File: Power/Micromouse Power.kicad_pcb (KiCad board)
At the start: 2 copper layers, 44.7 x 28.4 mm, 56 parts, among them J1 Battery, J2 Conn_02x08_Odd_Even, Q1 AO3401A, Q2 AO3401A, SW1 pwr, SW2 pwr, U1 AMS1117-3.3, U2 TP4056, U3 DRV8837, U4 DRV8837

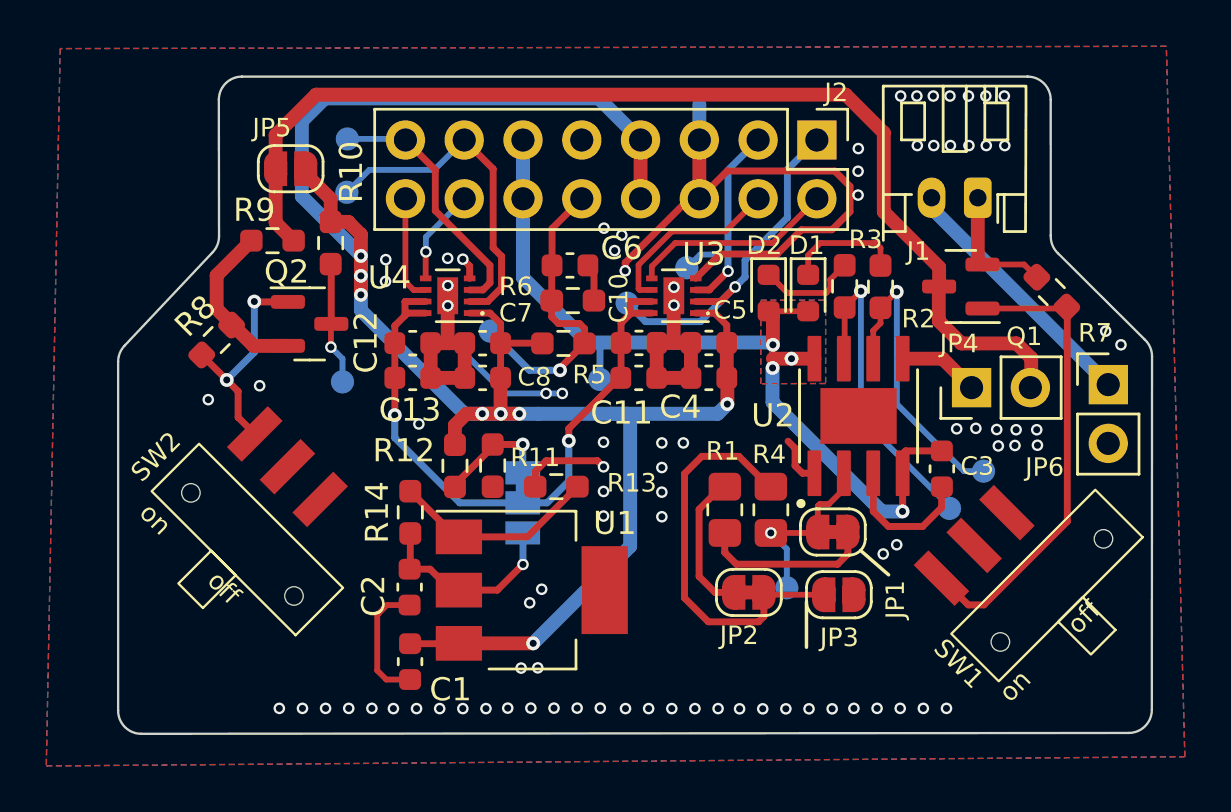
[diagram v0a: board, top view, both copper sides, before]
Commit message: Fixed tab width
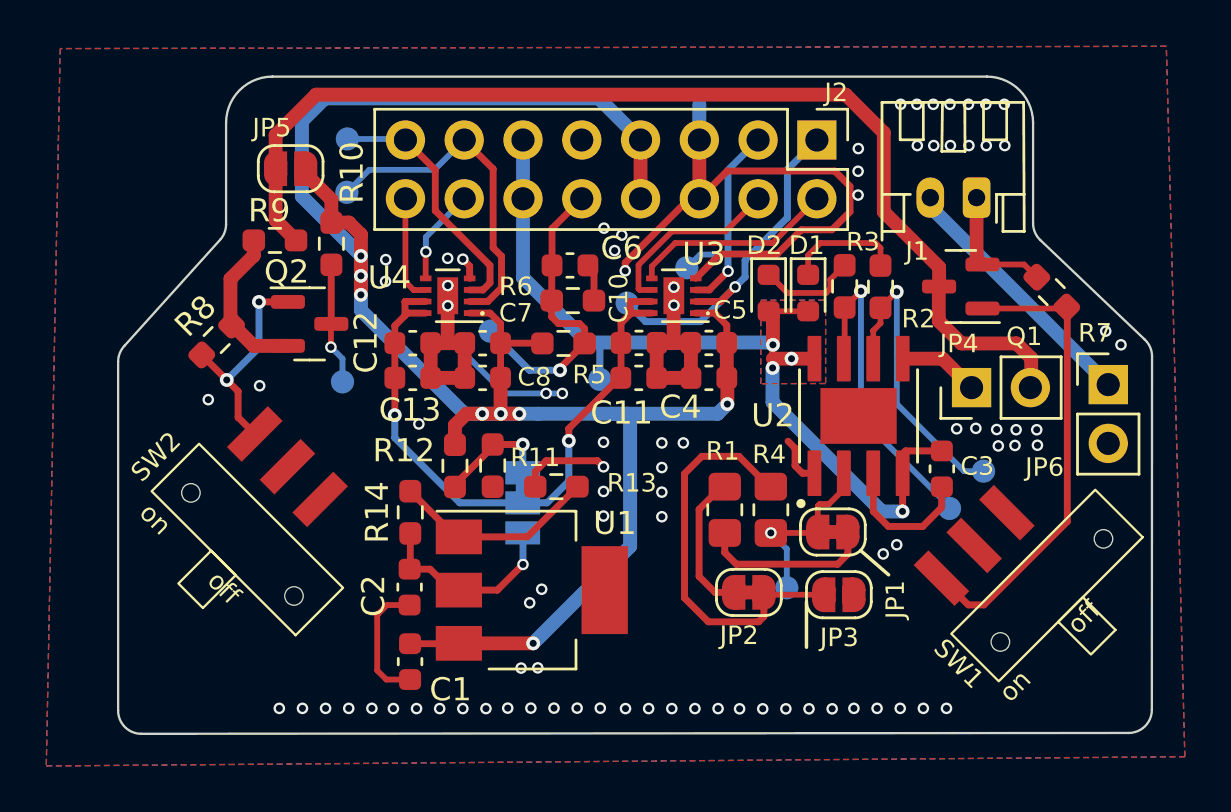
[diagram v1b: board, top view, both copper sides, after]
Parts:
- moved R9 0.11 mm to (146.2, 112.7)
- moved J1 0.06 mm to (176.5, 110.8)
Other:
- outline, holes or cut-outs redrawn

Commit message: Added student card to silkscreen
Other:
- board text added: "Montso Mokake (MKKMON002) Micromouse Power v0.0.0"
- board text removed: "Montso Mokake Micromouse Power v0.0.0"
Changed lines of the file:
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@@
   (gr_line (start 139.676911 117.244934) (end 143.812432 112.661786)
     (stroke (width 0.1) (type default)) (layer "Edge.Cuts"))
-  (gr_text "Montso  Mokake\nMicromouse Power v0.0.0" (at 183.49 132.18) (layer "B.SilkS")
+  (gr_text "Montso  Mokake (MKKMON002)\nMicromouse Power v0.0.0" (at 183.49 132.18) (layer "B.SilkS")
     (effects (font (size 1 1) (thickness 0.15)) (justify left bottom mirror))
   )
